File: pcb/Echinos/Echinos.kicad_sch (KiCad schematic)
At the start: 0 parts

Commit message: [PCB] - Save last state with Helios MCU board and gasket tabs on PCB.
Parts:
- added F2: 500mA, Fuse:Fuse_1206_3216Metric, symbol Device:Polyfuse
- added H1, H2, H3, H4, H5, H6: MountHole, MountingHole:MountingHole_3.2mm_M3_Pad, symbol Mechanical:MountingHole_Pad
- added J1, J2, J3: Conn_01x06_Socket, Connector_FFC-FPC:Hirose_FH12-6S-0.5SH_1x06-1MP_P0.50mm_Horizontal, symbol Connector:Conn_01x06_Socket
- added J4: ~, Connector_FFC-FPC:Hirose_FH12-12S-0.5SH_1x12-1MP_P0.50mm_Horizontal, symbol Vik:vik-keyboard-connector
- added J5: SATA-7p, Echinos:SATA_1x07_P1.27mm_pads_SMD, symbol Echinos:SATA-7p
- added JP0, JP11: SolderJumper_2_Bridged, Jumper:SolderJumper-2_P1.3mm_Bridged_Pad1.0x1.5mm, symbol Jumper:SolderJumper_2_Bridged
- added JP12: Jumper_3_Bridged12, Jumper:SolderJumper-3_P1.3mm_Bridged12_Pad1.0x1.5mm_NumberLabels, symbol Jumper:SolderJumper_3_Bridged12
- added JP13, JP14, JP15, JP16: Jumper_2_Open, Jumper:SolderJumper-2_P1.3mm_Open_Pad1.0x1.5mm, symbol Jumper:Jumper_2_Open
- added R13, R14, R15, R16: 4.7k, Resistor_SMD:R_0805_2012Metric_Pad1.20x1.40mm_HandSolder, symbol Device:R
- added S1, S2, S3, S4, S5, S6, S7: GasketSupport, Echinos:Gasket_Pad_15x3mm, symbol Mechanical:Mechanical_Shape
- added SW1: Reset, Button_Switch_SMD:SW_SPST_TL3342, symbol Switch:SW_Push
- added U1: Helios, Echinos:Helios_AH_USBdn, symbol PCM_marbastlib-promicroish:Helios
- added U7: SRV05-4, Package_TO_SOT_SMD:SOT-23-6, symbol Power_Protection:SRV05-4
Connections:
- net GND: now also H1.1, H2.1, H3.1, H4.1, H5.1, H6.1, J2.2 (Pin_2), J3.3 (Pin_3), J4.2 (GND), J5.1 (S1), J5.4 (S4), J5.7 (S7), J5.SH1 (SHIELD), J5.SH2 (SHIELD), SW1.1, U1.14 (GND), U1.3 (GND), U1.4 (GND), U7.2 (VN)
- new net: JP15.2 (B), R15.2
- new net: JP13.2 (B), R13.2
- new net: JP14.2 (B), R14.2
- new net: JP16.2 (B), R16.2
- new net: J4.6 (5V), JP0.2 (B)
- new net: JP11.2 (B), JP12.2 (C)
- new net +3.3V: J2.1 (Pin_1), J3.1 (Pin_1), J4.1 (3V3), JP13.1 (A), JP14.1 (A), JP15.1 (A), JP16.1 (A), U1.16 (3V3)
- new net +5V: F2.1, J3.2 (Pin_2), JP0.1 (A), U1.13 (5V)
- new net Backlight/backlight_in: JP12.1 (A)
- new net RX: J5.3 (S3), U1.2 (P1), U7.4 (IO3), U7.6 (IO4)
- new net TX: J5.2 (S2), U1.1 (P0), U7.1 (IO1), U7.3 (IO2)
- new net VBUS_split: F2.2, J5.5 (S5), J5.6 (S6), U7.5 (VP)
- new net adc_0: J2.3 (Pin_3), J4.7 (GP_AD1), U1.20 (P26)
- new net adc_1: J2.4 (Pin_4), J4.9 (GP_AD2), U1.19 (P27)
- new net col1: J1.2 (Pin_2), U1.29 (P16)
- new net col2: J1.3 (Pin_3), J2.6 (Pin_6), U1.8 (P5)
- new net col3: J1.4 (Pin_4), U1.7 (P4)
- new net col4: J1.5 (Pin_5), U1.6 (P3)
- new net col5: J1.6 (Pin_6), U1.5 (P2)
- new net csn1: J4.10 (SPI_CS), U1.24 (P21)
- new net miso1: J4.11 (MISO), U1.22 (P20)
- new net mosi1: J4.8 (MOSI), U1.23 (P23)
- new net ps2_clk: J3.5 (Pin_5), R16.1, U1.18 (P28)
- new net ps2_data: J3.4 (Pin_4), R15.1, U1.17 (P29)
- new net ps2_reset: J3.6 (Pin_6), U1.31 (P10)
- new net reset: SW1.2, U1.15 (RST)
- new net rgb: JP11.1 (A), U1.34 (P25)
- new net rgb_out: J4.5 (RGB_DO), JP12.3 (B)
- new net row1: U1.12 (P9)
- new net row2: U1.25 (P12)
- new net row3: U1.11 (P8)
- new net row4: U1.10 (P7)
- new net row5: U1.9 (P6)
- new net row6: J1.1 (Pin_1), U1.26 (P13)
- new net row7: J2.5 (Pin_5), U1.30 (P11)
- new net sck1: J4.12 (SCLK), U1.21 (P22)
- new net scl1: J4.4 (SCL), R14.1, U1.27 (P14)
- new net sda1: J4.3 (SDA), R13.1, U1.28 (P15)
- no-connect marks 0 -> 2
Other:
- removed sheet Left Side
- added sheet Backlight (LED_left.kicad_sch)
- added sheet Matrix (Keyboard_Matrix.kicad_sch)
- note added: ""adc_0" and "adc_1" lines are shared with VIK."
- note added: ""data" and "clk" are 3.3V logic."
- note added: "(optional) Can use RP2040 internal pull-ups"
- note added: "(optional) Level-shift logic is on modules."
- note added: "(optional) Pull-up should be on VIK modules."
- note added: "(optional) Reset logic is on modules."
- note added: "Bridge 23 to bipass the keyboard rgb"
- note added: "Case EMI Shield / mounting holes"
- note added: "Case Gasket mounts"
- note added: "Cut it to disable RGB"
- note added: "Diodes are on modules (ColumnToRow to avoid custom scanning)."
- note added: "ESD protection (USB + SATA)"
- note added: "Expansion connectors"
- note added: "Halves communication (SERIAL_USART_FULL_DUPLEX)"
- note added: "Helios specific - GPIO 25 is level shifted to 5V logic level (RGB) - GPIO 19 is VBUS detection - GPIO 18 is not connected / used - GPIO 24 is not connected / used - GPIO 17 is micro LED (user controlled) - Power LED (Red) disabled by default (can be bridged)"
- note added: "Information"
- note added: "Joysticks / ADC devices - KSilver-JP19 - Joycon - ..."
- note added: "Joysticks like JP19 can be mapped directly to keyboard matrix. (optional) Diodes are on modules."
- note added: "Keyboard RGB (leds)"
- note added: "Keyboard matrix (Keys)"
- note added: "Matrix expansion - 5-way Navigation switch - Mouse buttons - ..."
- note added: "On board MCU reset"
- note added: "Overcurrent protection"
- note added: "Packaging (metric | imperial) - Resistors - RP2040 --> 1005 | 0402 - USB data --> 1005 | 0402 - I2C puller --> 1005 | 0402 - Others --> 1608 | 0603 - Capacitors - RP2040 --> 1005 | 0402 - Others --> 1608 | 0603 - Diodes - Switches --> SOD-123 - TVS --> SOD-523 - Transistors - ESD --> SOT-723"
- note added: "RP2040"
- note added: "This jumper is not standard and is *not* required. Cut it if one want to connect a cirque trackpad directly via SPI."
- note added: "Trackpoints and PS/2 devices"
- note added: "USART full duplex RX_left <-- TX_right TX_left --> RX_right"
- note added: "VIK compatible (https://github.com/sadekbaroudi/vik) - Cirque compatible with FPC Type A cable (reverse pins)"
- note added: "VIK connector (SPI 1 / I2C 0)"
- note added: "With STM32 MCUs one can swap Rx and Tx at the software level --> Adding hardware selection is optionnal https://docs.qmk.fm/drivers/serial#setup-2"

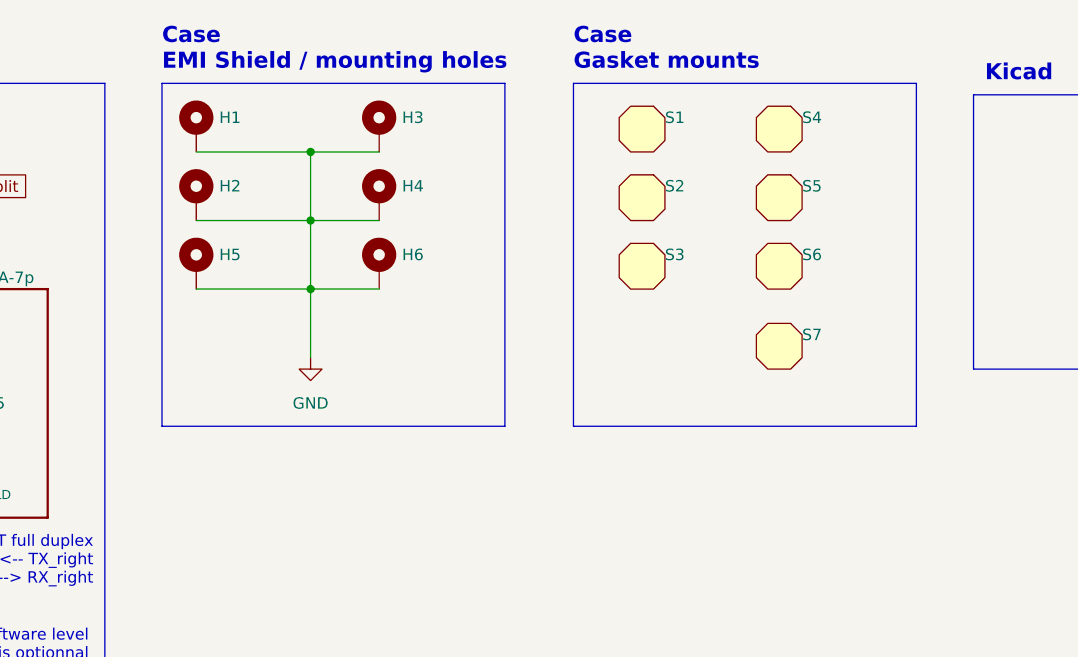
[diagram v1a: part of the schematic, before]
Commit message: [PCB] - Save last state with Helios MCU board (no gasket on PCB).
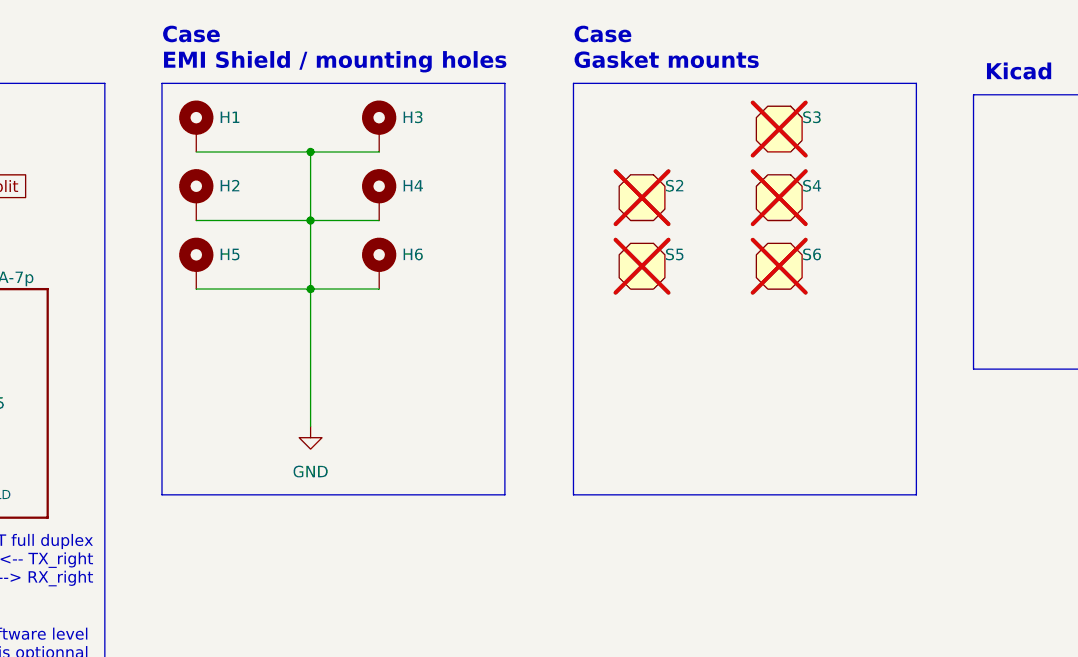
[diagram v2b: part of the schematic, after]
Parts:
- removed S1, S7: GasketSupport, Echinos:Gasket_Pad_15x3mm, symbol Mechanical:Mechanical_Shape
- S2, S3, S4, S5, S6: footprint Echinos:Gasket_Pad_15x3mm -> Echinos:EarCut_8mm; now not fitted
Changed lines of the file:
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@@
 	(rectangle
 		(start 177.8 22.86)
-		(end 215.9 60.96)
+		(end 215.9 68.58)
 		(stroke
 			(width 0)
@@
 	(rectangle
 		(start 132.08 22.86)
-		(end 170.18 60.96)
+		(end 170.18 68.58)
 		(stroke
 			(width 0)
@@
 	(wire
 		(pts
+			(xy 148.59 45.72) (xy 148.59 60.96)
+		)
+		(stroke
+			(width 0)
+			(type default)
+		)
+	)
+	(wire
+		(pts
 			(xy 379.73 67.31) (xy 369.57 67.31)
 		)
@@
 	(wire
 		(pts
-			(xy 148.59 45.72) (xy 148.59 53.34)
-		)
-		(stroke
-			(width 0)
-			(type default)
-		)
-	)
-	(wire
-		(pts
 			(xy 64.77 222.25) (xy 77.47 222.25)
 		)
@@
 	(symbol
 		(lib_id "Mechanical:Mechanical_Shape")
-		(at 200.66 35.56 0)
+		(at 185.42 43.18 0)
 		(unit 1)
 		(exclude_from_sim yes)
 		(in_bom no)
-		(on_board yes)
-		(dnp no)
+		(on_board no)
+		(dnp yes)
 		(property "Reference" "S5"
-			(at 203.2 34.29 0)
+			(at 187.96 41.91 0)
 			(effects
 				(font
@@
 		)
 		(property "Value" "GasketSupport"
-			(at 203.2 35.56 0)
+			(at 187.96 43.18 0)
 			(effects
 				(font
@@
 			)
 		)
-		(property "Footprint" "Echinos:Gasket_Pad_15x3mm"
-			(at 200.66 40.64 0)
+		(property "Footprint" "Echinos:EarCut_8mm"
+			(at 185.42 48.26 0)
 			(effects
 				(font
@@
 		)
 		(property "Datasheet" "~"
-			(at 200.66 31.75 0)
+			(at 185.42 39.37 0)
 			(effects
 				(font
@@
 		)
 		(property "Description" "Mechanical shape, non-electric, board outlines"
-			(at 200.66 35.56 0)
+			(at 185.42 43.18 0)
 			(effects
 				(font
@@
 		)
 		(property "FT Layer Override" ""
-			(at 200.66 35.56 0)
+			(at 185.42 43.18 0)
 			(effects
 				(font
@@
 		)
 		(property "FT Position Offset" ""
-			(at 200.66 35.56 0)
+			(at 185.42 43.18 0)
 			(effects
 				(font
@@
 	)
 	(symbol
-		(lib_id "Mechanical:Mechanical_Shape")
-		(at 185.42 27.94 0)
-		(unit 1)
-		(exclude_from_sim yes)
-		(in_bom no)
-		(on_board yes)
-		(dnp no)
-		(property "Reference" "S1"
-			(at 187.96 26.67 0)
-			(effects
-				(font
-					(size 1.27 1.27)
-				)
-				(justify left)
-			)
-		)
-		(property "Value" "GasketSupport"
-			(at 187.96 27.94 0)
-			(effects
-				(font
-					(size 1.27 1.27)
-				)
-				(justify left)
-				(hide yes)
-			)
-		)
-		(property "Footprint" "Echinos:Gasket_Pad_15x3mm"
-			(at 185.42 33.02 0)
-			(effects
-				(font
-					(size 1.27 1.27)
-				)
-				(hide yes)
-			)
-		)
-		(property "Datasheet" "~"
-			(at 185.42 24.13 0)
-			(effects
-				(font
-					(size 1.27 1.27)
-				)
-				(hide yes)
-			)
-		)
-		(property "Description" "Mechanical shape, non-electric, board outlines"
-			(at 185.42 27.94 0)
-			(effects
-				(font
-					(size 1.27 1.27)
-				)
-				(hide yes)
-			)
-		)
-		(property "FT Layer Override" ""
-			(at 185.42 27.94 0)
-			(effects
-				(font
-					(size 1.27 1.27)
-				)
-				(hide yes)
-			)
-		)
-		(property "FT Position Offset" ""
-			(at 185.42 27.94 0)
-			(effects
-				(font
-					(size 1.27 1.27)
-				)
-				(hide yes)
-			)
-		)
-		(instances
-			(project "Echinos"
-				(path "/5bd3006d-ec09-4ffb-bec3-03fa5613b46a"
-					(reference "S1")
-					(unit 1)
-				)
-			)
-		)
-	)
-	(symbol
 		(lib_id "Connector:Conn_01x06_Socket")
 		(at 102.87 193.04 0)
@@
 	(symbol
 		(lib_id "power:GND")
-		(at 148.59 53.34 0)
+		(at 148.59 60.96 0)
 		(unit 1)
 		(exclude_from_sim no)
@@
 		(fields_autoplaced yes)
 		(property "Reference" "#PWR053"
-			(at 148.59 59.69 0)
+			(at 148.59 67.31 0)
 			(effects
 				(font
@@
 		)
 		(property "Value" "GND"
-			(at 148.59 58.42 0)
+			(at 148.59 66.04 0)
 			(effects
 				(font
@@
 		)
 		(property "Footprint" ""
-			(at 148.59 53.34 0)
+			(at 148.59 60.96 0)
 			(effects
 				(font
@@
 		)
 		(property "Datasheet" ""
-			(at 148.59 53.34 0)
+			(at 148.59 60.96 0)
 			(effects
 				(font
@@
 		)
 		(property "Description" ""
-			(at 148.59 53.34 0)
+			(at 148.59 60.96 0)
 			(effects
 				(font
@@
 	)
 	(symbol
-		(lib_id "Mechanical:Mechanical_Shape")
-		(at 200.66 52.07 0)
-		(unit 1)
-		(exclude_from_sim yes)
-		(in_bom no)
-		(on_board yes)
-		(dnp no)
-		(property "Reference" "S7"
-			(at 203.2 50.8 0)
-			(effects
-				(font
-					(size 1.27 1.27)
-				)
-				(justify left)
-			)
-		)
-		(property "Value" "GasketSupport"
-			(at 203.2 52.07 0)
-			(effects
-				(font
-					(size 1.27 1.27)
-				)
-				(justify left)
-				(hide yes)
-			)
-		)
-		(property "Footprint" "Echinos:Gasket_Pad_15x3mm"
-			(at 200.66 57.15 0)
-			(effects
-				(font
-					(size 1.27 1.27)
-				)
-				(hide yes)
-			)
-		)
-		(property "Datasheet" "~"
-			(at 200.66 48.26 0)
-			(effects
-				(font
-					(size 1.27 1.27)
-				)
-				(hide yes)
-			)
-		)
-		(property "Description" "Mechanical shape, non-electric, board outlines"
-			(at 200.66 52.07 0)
-			(effects
-				(font
-					(size 1.27 1.27)
-				)
-				(hide yes)
-			)
-		)
-		(property "FT Layer Override" ""
-			(at 200.66 52.07 0)
-			(effects
-				(font
-					(size 1.27 1.27)
-				)
-				(hide yes)
-			)
-		)
-		(property "FT Position Offset" ""
-			(at 200.66 52.07 0)
-			(effects
-				(font
-					(size 1.27 1.27)
-				)
-				(hide yes)
-			)
-		)
-		(instances
-			(project "Echinos"
-				(path "/5bd3006d-ec09-4ffb-bec3-03fa5613b46a"
-					(reference "S7")
-					(unit 1)
-				)
-			)
-		)
-	)
-	(symbol
 		(lib_id "power:+3.3V")
 		(at 198.12 261.62 0)
@@
 	(symbol
 		(lib_id "Mechanical:Mechanical_Shape")
-		(at 185.42 43.18 0)
+		(at 200.66 27.94 0)
 		(unit 1)
 		(exclude_from_sim yes)
 		(in_bom no)
-		(on_board yes)
-		(dnp no)
+		(on_board no)
+		(dnp yes)
 		(property "Reference" "S3"
-			(at 187.96 41.91 0)
+			(at 203.2 26.67 0)
 			(effects
 				(font
@@
 		)
 		(property "Value" "GasketSupport"
-			(at 187.96 43.18 0)
+			(at 203.2 27.94 0)
 			(effects
 				(font
@@
 			)
 		)
-		(property "Footprint" "Echinos:Gasket_Pad_15x3mm"
-			(at 185.42 48.26 0)
+		(property "Footprint" "Echinos:EarCut_8mm"
+			(at 200.66 33.02 0)
 			(effects
 				(font
@@
 		)
 		(property "Datasheet" "~"
-			(at 185.42 39.37 0)
+			(at 200.66 24.13 0)
 			(effects
 				(font
@@
 		)
 		(property "Description" "Mechanical shape, non-electric, board outlines"
-			(at 185.42 43.18 0)
+			(at 200.66 27.94 0)
 			(effects
 				(font
@@
 		)
 		(property "FT Layer Override" ""
-			(at 185.42 43.18 0)
+			(at 200.66 27.94 0)
 			(effects
 				(font
@@
 		)
 		(property "FT Position Offset" ""
-			(at 185.42 43.18 0)
+			(at 200.66 27.94 0)
 			(effects
 				(font
@@
 	(symbol
 		(lib_id "Mechanical:Mechanical_Shape")
-		(at 200.66 27.94 0)
+		(at 200.66 35.56 0)
 		(unit 1)
 		(exclude_from_sim yes)
 		(in_bom no)
-		(on_board yes)
-		(dnp no)
+		(on_board no)
+		(dnp yes)
 		(property "Reference" "S4"
-			(at 203.2 26.67 0)
+			(at 203.2 34.29 0)
 			(effects
 				(font
@@
 		)
 		(property "Value" "GasketSupport"
-			(at 203.2 27.94 0)
+			(at 203.2 35.56 0)
 			(effects
 				(font
@@
 			)
 		)
-		(property "Footprint" "Echinos:Gasket_Pad_15x3mm"
-			(at 200.66 33.02 0)
+		(property "Footprint" "Echinos:EarCut_8mm"
+			(at 200.66 40.64 0)
 			(effects
 				(font
@@
 		)
 		(property "Datasheet" "~"
-			(at 200.66 24.13 0)
+			(at 200.66 31.75 0)
 			(effects
 				(font
@@
 		)
 		(property "Description" "Mechanical shape, non-electric, board outlines"
-			(at 200.66 27.94 0)
+			(at 200.66 35.56 0)
 			(effects
 				(font
@@
 		)
 		(property "FT Layer Override" ""
-			(at 200.66 27.94 0)
+			(at 200.66 35.56 0)
 			(effects
 				(font
@@
 		)
 		(property "FT Position Offset" ""
-			(at 200.66 27.94 0)
+			(at 200.66 35.56 0)
 			(effects
 				(font
@@
 		(exclude_from_sim yes)
 		(in_bom no)
-		(on_board yes)
-		(dnp no)
+		(on_board no)
+		(dnp yes)
 		(property "Reference" "S6"
 			(at 203.2 41.91 0)
@@
 			)
 		)
-		(property "Footprint" "Echinos:Gasket_Pad_15x3mm"
+		(property "Footprint" "Echinos:EarCut_8mm"
 			(at 200.66 48.26 0)
 			(effects
@@
 		(exclude_from_sim yes)
 		(in_bom no)
-		(on_board yes)
-		(dnp no)
+		(on_board no)
+		(dnp yes)
 		(property "Reference" "S2"
 			(at 187.96 34.29 0)
@@
 			)
 		)
-		(property "Footprint" "Echinos:Gasket_Pad_15x3mm"
+		(property "Footprint" "Echinos:EarCut_8mm"
 			(at 185.42 40.64 0)
 			(effects

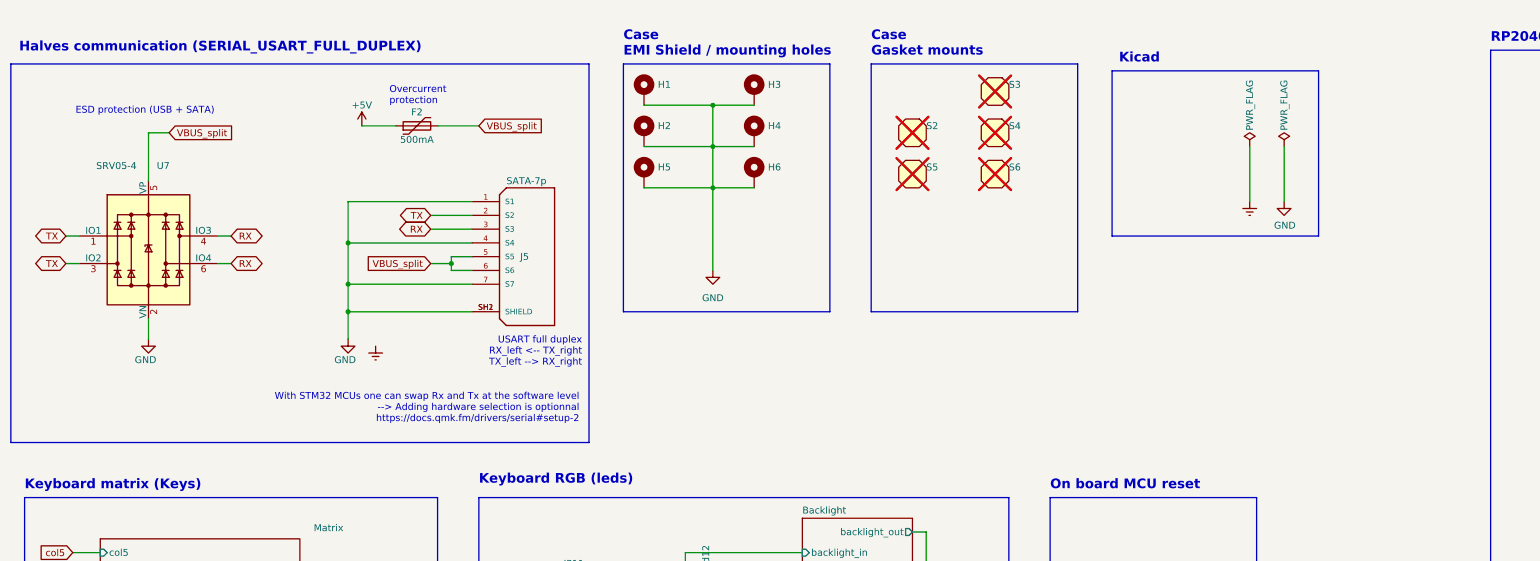
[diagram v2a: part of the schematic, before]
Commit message: [PCB] - Save last state with Helios MCU board. Add multiple choices for split communication. Also fix SATA footprint and rework board (helios) holes to be smaller (0.9 --> 0.825) to be able to use spring loaded pins. Currently supported split communication are:   - SATA (data)   - USB-B (micro)   - Direct wires to whatever using 2.0 pitch header
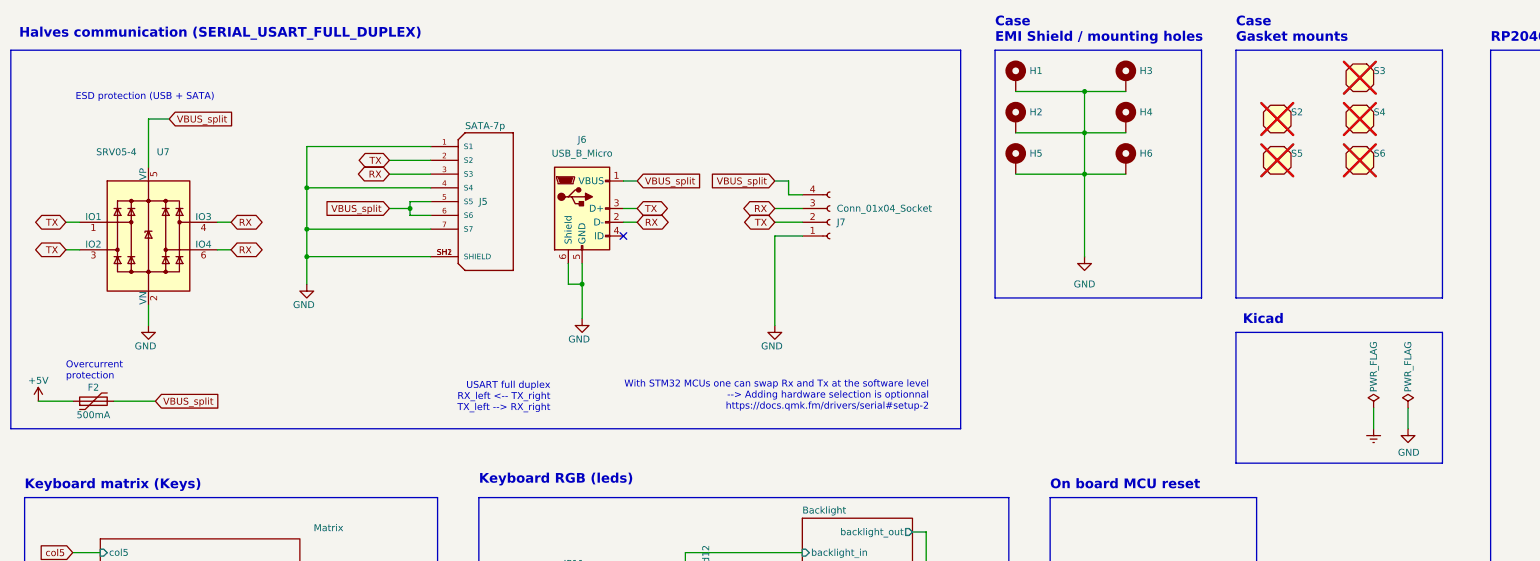
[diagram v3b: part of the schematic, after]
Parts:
- added J6: USB_B_Micro, Echinos:USB_Micro-B_type5_Amphenol_Horizontal, symbol Connector:USB_B_Micro
- added J7: Conn_01x04_Socket, Connector_PinHeader_2.00mm:PinHeader_1x04_P2.00mm_Vertical, symbol Connector:Conn_01x04_Socket
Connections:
- net GND: now also J6.5 (GND), J6.6 (Shield), J7.1 (Pin_1)
- net RX: now also J6.2 (D-), J7.3 (Pin_3)
- net TX: now also J6.3 (D+), J7.2 (Pin_2)
- net VBUS_split: now also J6.1 (VBUS), J7.4 (Pin_4)
- no-connect marks 2 -> 3
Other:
- moved on the sheet: F2, H1, H2, H3, H4, H5, H6, J5, S2, S3, S4, S5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
